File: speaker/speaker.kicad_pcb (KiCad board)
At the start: 2 copper layers, 68.5 x 55.2 mm, 33 parts, among them J2 JST Battery, J3 Speaker Output Pins, U1 PicoW, U2 MAX40203AUK+T, U3 MAX98357AETE_T, U4 MAX16054AZT_T

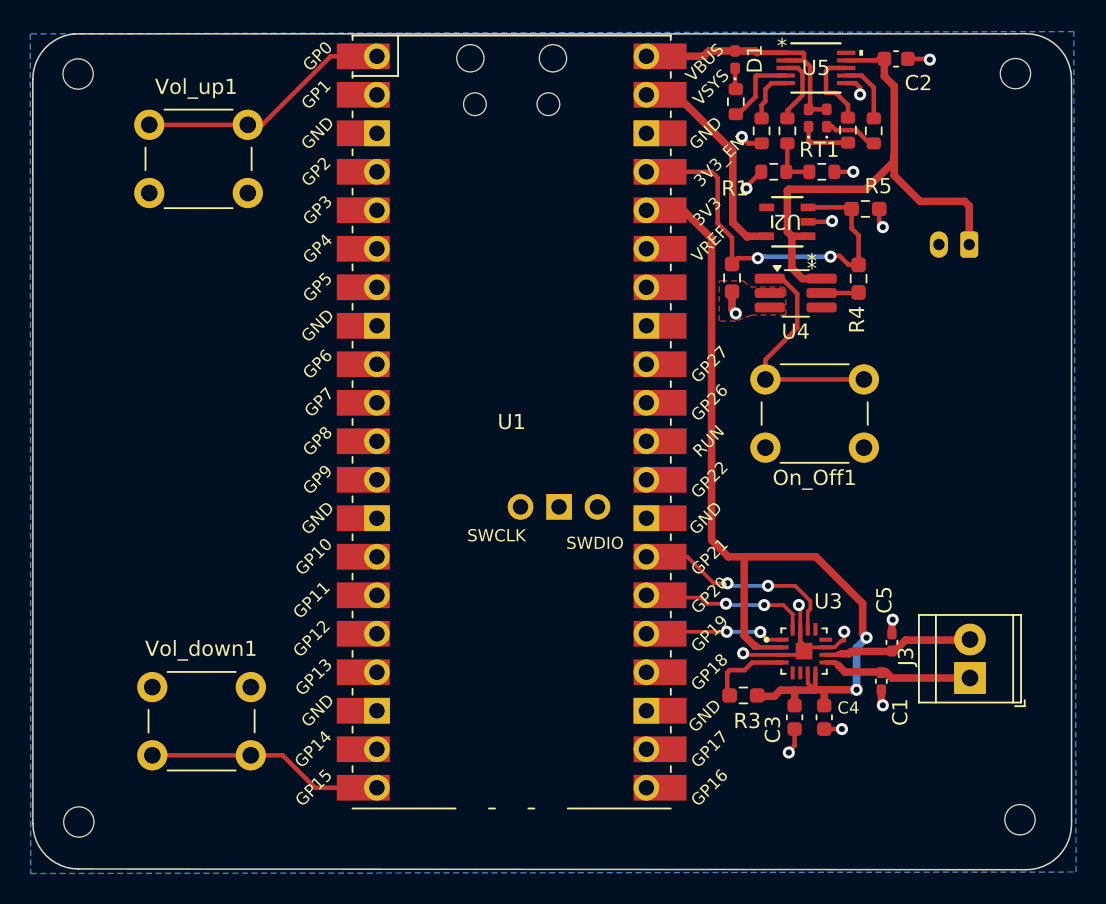
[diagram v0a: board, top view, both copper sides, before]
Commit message: add header
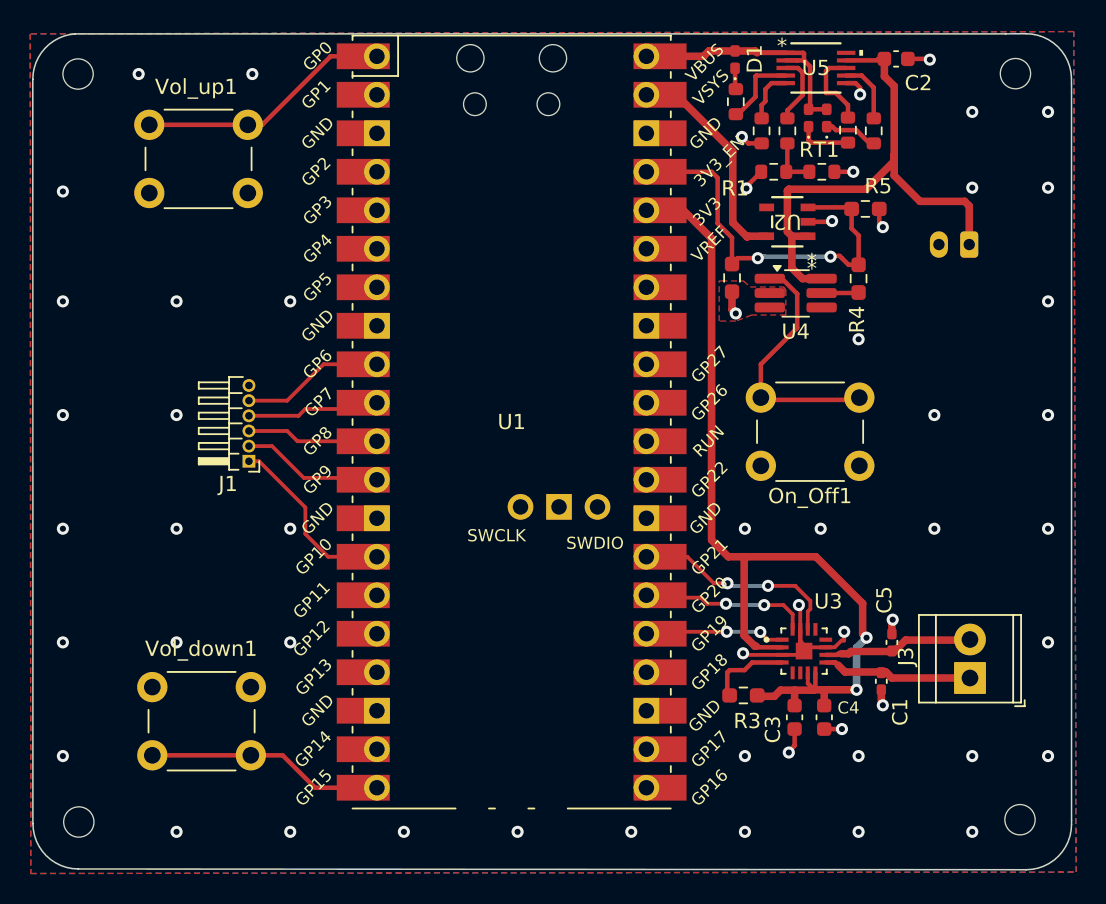
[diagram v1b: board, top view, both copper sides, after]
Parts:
- added J1: Conn_01x06_Pin, Connector_PinHeader_1.00mm:PinHeader_1x06_P1.00mm_Horizontal, F.Cu at (92.3, 90.5)
- moved On_Off1 1.24 mm to (132.6, 90.8)
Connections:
- U1 pad 10: unconnected-(U1-GPIO7-Pad10) -> Net-(J1-Pin_4)
- U1 pad 11: unconnected-(U1-GPIO8-Pad11) -> Net-(J1-Pin_3)
- U1 pad 12: unconnected-(U1-GPIO9-Pad12)_1 -> Net-(J1-Pin_2)
- U1 pad 14: unconnected-(U1-GPIO10-Pad14)_1 -> Net-(J1-Pin_1)
- U1 pad 3: unconnected-(U1-GND-Pad3) -> GND
- U1 pad 9: unconnected-(U1-GPIO6-Pad9) -> Net-(J1-Pin_5)
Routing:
- net Net-(J1-Pin_1): track 0.00 -> 12.1 mm
- net Net-(J1-Pin_5): track 0.00 -> 9.44 mm
- net Net-(J1-Pin_2): track 0.00 -> 9.36 mm
- net Net-(J1-Pin_4): track 0.00 -> 8.80 mm
- net Net-(J1-Pin_3): track 0.00 -> 8.73 mm
- net Net-(On_Off1-B): track 15.2 -> 16.7 mm
- net GND: vias 15 -> 55

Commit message: update schematic
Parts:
- D1: value LED -> LED_GREEN
- D2: value LED -> LED_ORANGE
- D3: value LED -> LED_RED
- U5: value ~ -> MCP73833
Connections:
- U1 pad 1: Net-(U1-GPIO0) -> unconnected-(U1-GPIO0-Pad1)
- U1 pad 2: unconnected-(U1-GPIO1-Pad2)_1 -> Net-(U1-GPIO1)
- Vol_up1 pad 2: Net-(U1-GPIO0) -> Net-(U1-GPIO1)
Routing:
- net Net-(U1-GPIO0): track 16.9 -> 0.00 mm
- net Net-(U1-GPIO1): track 0.00 -> 16.8 mm

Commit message: add power led
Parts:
- added D4: LED_BLUE, LED_SMD:LED_0402_1005Metric_Pad0.77x0.64mm_HandSolder, F.Cu at (136.5, 91.0)
- added R_POWER_LED1: 1K, Resistor_SMD:R_0603_1608Metric, F.Cu at (136.5, 89.2)
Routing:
- net +3V3: track 62.5 -> 71.8 mm
- net Net-(D4-K): track 0.00 -> 1.38 mm
- net GND: vias 55 -> 52

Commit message: changed footprint for battery connector
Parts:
- J2: footprint Connector_JST:JST_PH_S2B-PH-K_1x02_P2.00mm_Horizontal -> Connector_JST:JST_PH_S2B-PH-SM4-TB_1x02-1MP_P2.00mm_Horizontal
- moved J2 1.14 mm to (140.1, 75.2)
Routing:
- net GND: track 31.0 -> 36.0 mm
- net /V_LOAD: track 36.1 -> 37.3 mm, vias 0 -> 1
